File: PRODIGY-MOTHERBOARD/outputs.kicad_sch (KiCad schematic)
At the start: 37 parts, among them J10 RTD_PT100, J11 Can, J12 USB_A, J13 SPI_OUT, J14 MOTOR, J15 12V OUT, J16 Neopixel, J17 SERIAL, J18 I2C, J9 A_IN, U6 PCA9306DC

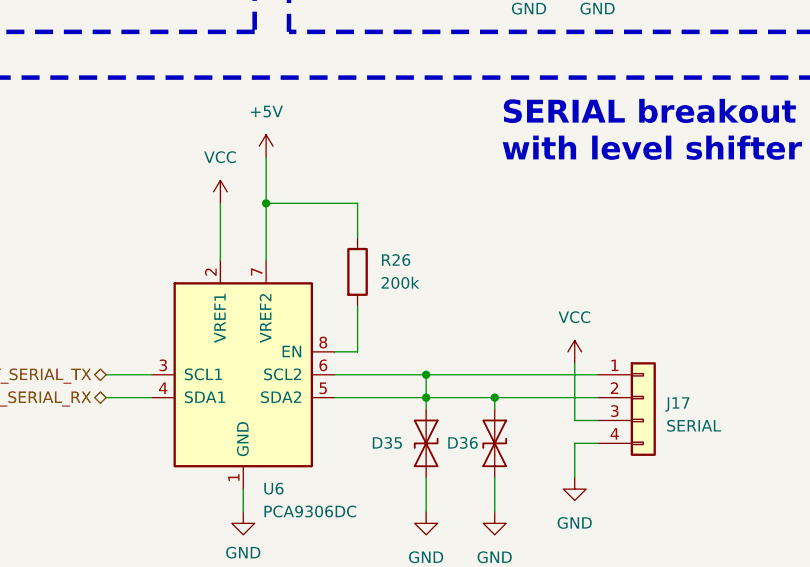
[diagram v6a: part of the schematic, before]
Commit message: finished motherboard bom and updated footprints
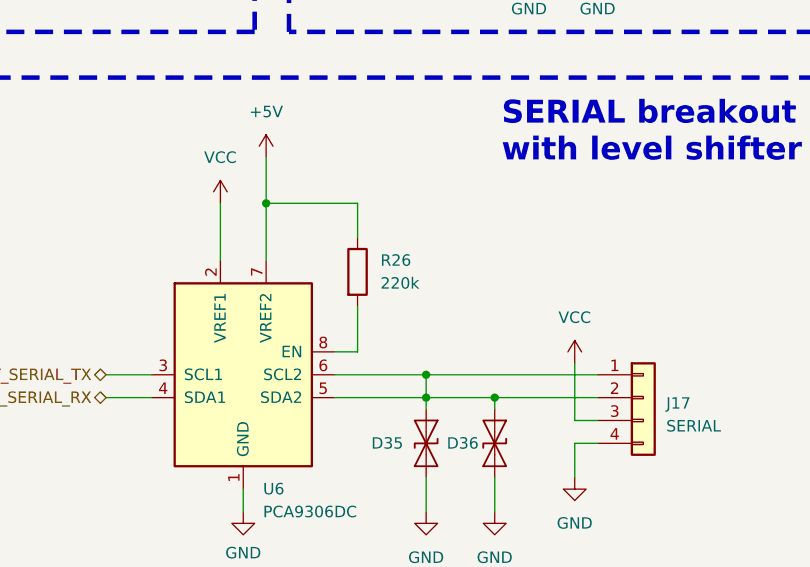
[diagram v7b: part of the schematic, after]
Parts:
- D14, D15, D16, D17, D18, D19, D20, D21, D22, D23, D24, D25, D26, D27, D28, D29, D30, D31, D32, D33, D34, D35, D36, D37, D38: TME (none) -> SD05.TCT
- J10, J11, J13, J14, J15, J16, J17, J18, J9: TME (none) -> DG308-2.54-02P
- J12: MOUSER (none) -> 649-87583-0010RHLF
- R26: value 200k -> 220k; TME (none) -> ERJ3EKF2203V
- U6: TME (none) -> PCA9306DCTR
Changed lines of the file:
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@@
 			)
 		)
-		(property "TME" ""
+		(property "TME" "SD05.TCT "
 			(at 241.3 104.14 0)
 			(effects
@@
 			)
 		)
-		(property "TME" ""
+		(property "TME" "SD05.TCT "
 			(at 134.62 143.51 0)
 			(effects
@@
 			)
 		)
-		(property "TME" ""
+		(property "TME" "SD05.TCT "
 			(at 119.38 44.45 0)
 			(effects
@@
 			)
 		)
-		(property "TME" ""
+		(property "TME" "SD05.TCT "
 			(at 233.68 104.14 0)
 			(effects
@@
 			)
 		)
-		(property "TME" ""
+		(property "TME" "DG308-2.54-02P"
 			(at 158.75 129.54 0)
 			(effects
@@
 			)
 		)
-		(property "MOUSER" ""
+		(property "MOUSER" " 649-87583-0010RHLF "
 			(at 153.67 80.01 0)
 			(effects
@@
 			)
 		)
-		(property "TME" ""
+		(property "TME" "SD05.TCT "
 			(at 52.07 82.55 0)
 			(effects
@@
 			)
 		)
-		(property "Value" "200k"
+		(property "Value" "220k"
 			(at 228.6 86.3599 0)
 			(effects
@@
 			)
 		)
-		(property "TME" ""
+		(property "TME" "ERJ3EKF2203V"
 			(at 226.06 85.09 0)
 			(effects
@@
 			)
 		)
-		(property "TME" ""
+		(property "TME" "SD05.TCT "
 			(at 139.7 44.45 0)
 			(effects
@@
 			)
 		)
-		(property "TME" ""
+		(property "TME" "SD05.TCT "
 			(at 54.61 40.64 0)
 			(effects
@@
 			)
 		)
-		(property "TME" ""
+		(property "TME" "SD05.TCT "
 			(at 128.27 90.17 0)
 			(effects
@@
 			)
 		)
-		(property "TME" ""
+		(property "TME" "SD05.TCT "
 			(at 60.96 40.64 0)
 			(effects
@@
 			)
 		)
-		(property "TME" ""
+		(property "TME" "DG308-2.54-02P"
 			(at 269.24 38.1 0)
 			(effects
@@
 			)
 		)
-		(property "TME" ""
+		(property "TME" "SD05.TCT "
 			(at 119.38 90.17 0)
 			(effects
@@
 			)
 		)
-		(property "TME" ""
+		(property "TME" "DG308-2.54-02P"
 			(at 67.31 71.12 0)
 			(effects
@@
 			)
 		)
-		(property "TME" ""
+		(property "TME" "DG308-2.54-02P"
 			(at 200.66 36.83 0)
 			(effects
@@
 			)
 		)
-		(property "TME" ""
+		(property "TME" "SD05.TCT "
 			(at 142.24 143.51 0)
 			(effects
@@
 			)
 		)
-		(property "TME" ""
+		(property "TME" "SD05.TCT "
 			(at 134.62 90.17 0)
 			(effects
@@
 			)
 		)
-		(property "TME" ""
+		(property "TME" "DG308-2.54-02P"
 			(at 71.12 123.19 0)
 			(effects
@@
 			)
 		)
-		(property "TME" ""
+		(property "TME" "DG308-2.54-02P"
 			(at 66.04 29.21 0)
 			(effects
@@
 			)
 		)
-		(property "TME" ""
+		(property "TME" "SD05.TCT "
 			(at 49.53 129.54 0)
 			(effects
@@
 			)
 		)
-		(property "TME" ""
+		(property "TME" "SD05.TCT "
 			(at 252.73 43.18 0)
 			(effects
@@
 			)
 		)
-		(property "TME" ""
+		(property "TME" "SD05.TCT "
 			(at 46.99 82.55 0)
 			(effects
@@
 			)
 		)
-		(property "TME" ""
+		(property "TME" "SD05.TCT "
 			(at 245.11 43.18 0)
 			(effects
@@
 			)
 		)
-		(property "TME" ""
+		(property "TME" "SD05.TCT "
 			(at 129.54 143.51 0)
 			(effects
@@
 			)
 		)
-		(property "TME" ""
+		(property "TME" "SD05.TCT "
 			(at 121.92 143.51 0)
 			(effects
@@
 			)
 		)
-		(property "TME" ""
+		(property "TME" "DG308-2.54-02P"
 			(at 156.21 34.29 0)
 			(effects
@@
 			)
 		)
-		(property "TME" ""
+		(property "TME" "SD05.TCT "
 			(at 39.37 82.55 0)
 			(effects
@@
 			)
 		)
-		(property "TME" ""
+		(property "TME" "SD05.TCT "
 			(at 207.01 146.05 0)
 			(effects
@@
 			)
 		)
-		(property "TME" ""
+		(property "TME" "SD05.TCT "
 			(at 132.08 44.45 0)
 			(effects
@@
 			)
 		)
-		(property "TME" ""
+		(property "TME" "DG308-2.54-02P"
 			(at 224.79 143.51 0)
 			(effects
@@
 			)
 		)
-		(property "TME" ""
+		(property "TME" "SD05.TCT "
 			(at 127 44.45 0)
 			(effects
@@
 			)
 		)
-		(property "TME" ""
+		(property "TME" "DG308-2.54-02P"
 			(at 257.81 99.06 0)
 			(effects
@@
 			)
 		)
-		(property "TME" ""
+		(property "TME" "PCA9306DCTR"
 			(at 213.36 96.52 0)
 			(effects
@@
 			)
 		)
-		(property "TME" ""
+		(property "TME" "SD05.TCT "
 			(at 57.15 129.54 0)
 			(effects
@@
 			)
 		)
-		(property "TME" ""
+		(property "TME" "SD05.TCT "
 			(at 59.69 82.55 0)
 			(effects
@@
 			)
 		)
-		(property "TME" ""
+		(property "TME" "SD05.TCT "
 			(at 190.5 41.91 0)
 			(effects
